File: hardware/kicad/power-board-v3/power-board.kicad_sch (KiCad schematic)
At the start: 5 parts

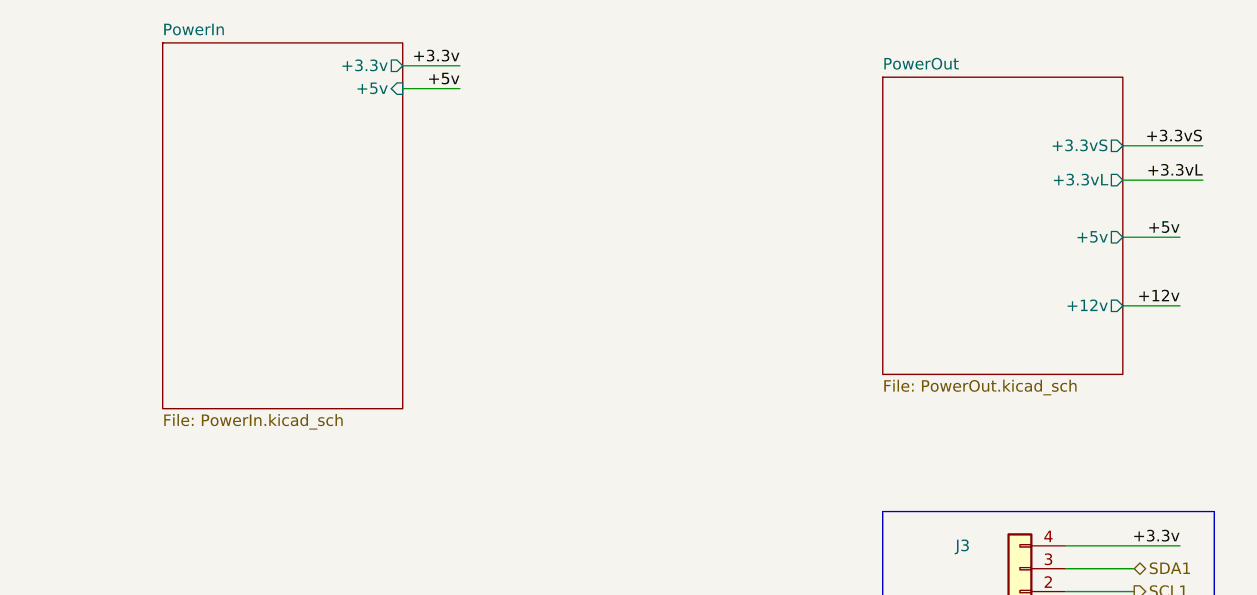
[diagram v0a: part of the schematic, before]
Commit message: add power balance and regulator
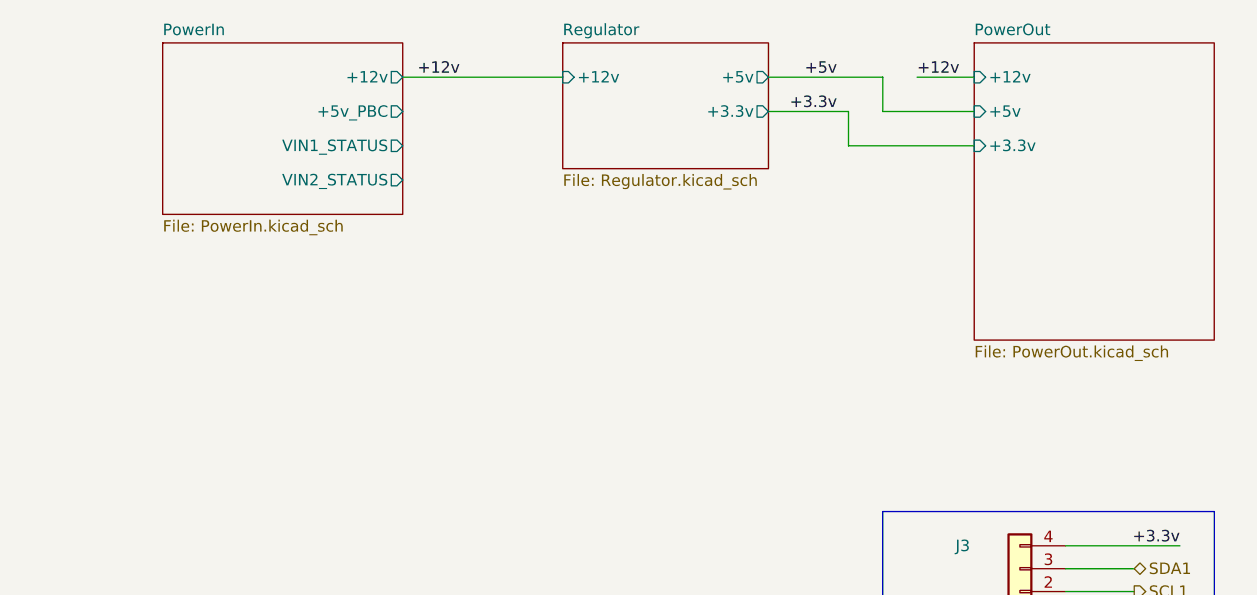
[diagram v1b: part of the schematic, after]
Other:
- added sheet Regulator (Regulator.kicad_sch)
- sheet PowerIn ports: added +12v, +5v_PBC, VIN1_STATUS, VIN2_STATUS; removed +3.3v, +5v
- sheet PowerOut ports: added +3.3v; removed +3.3vL, +3.3vS

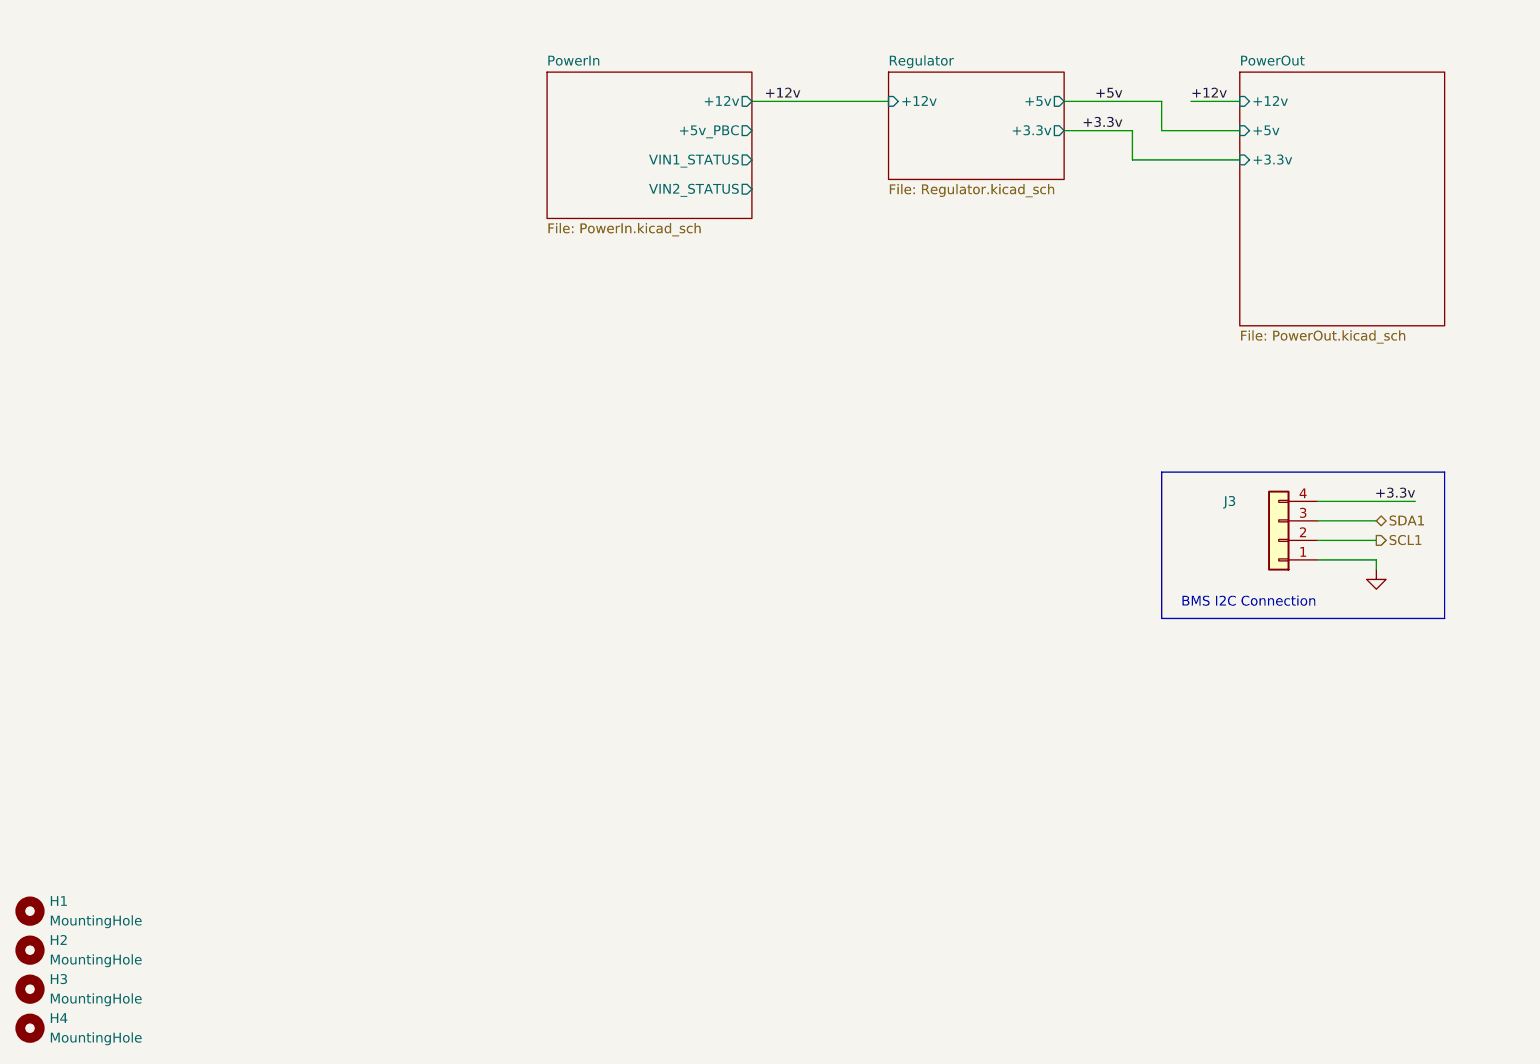
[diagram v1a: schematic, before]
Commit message: add base symbol and wiring
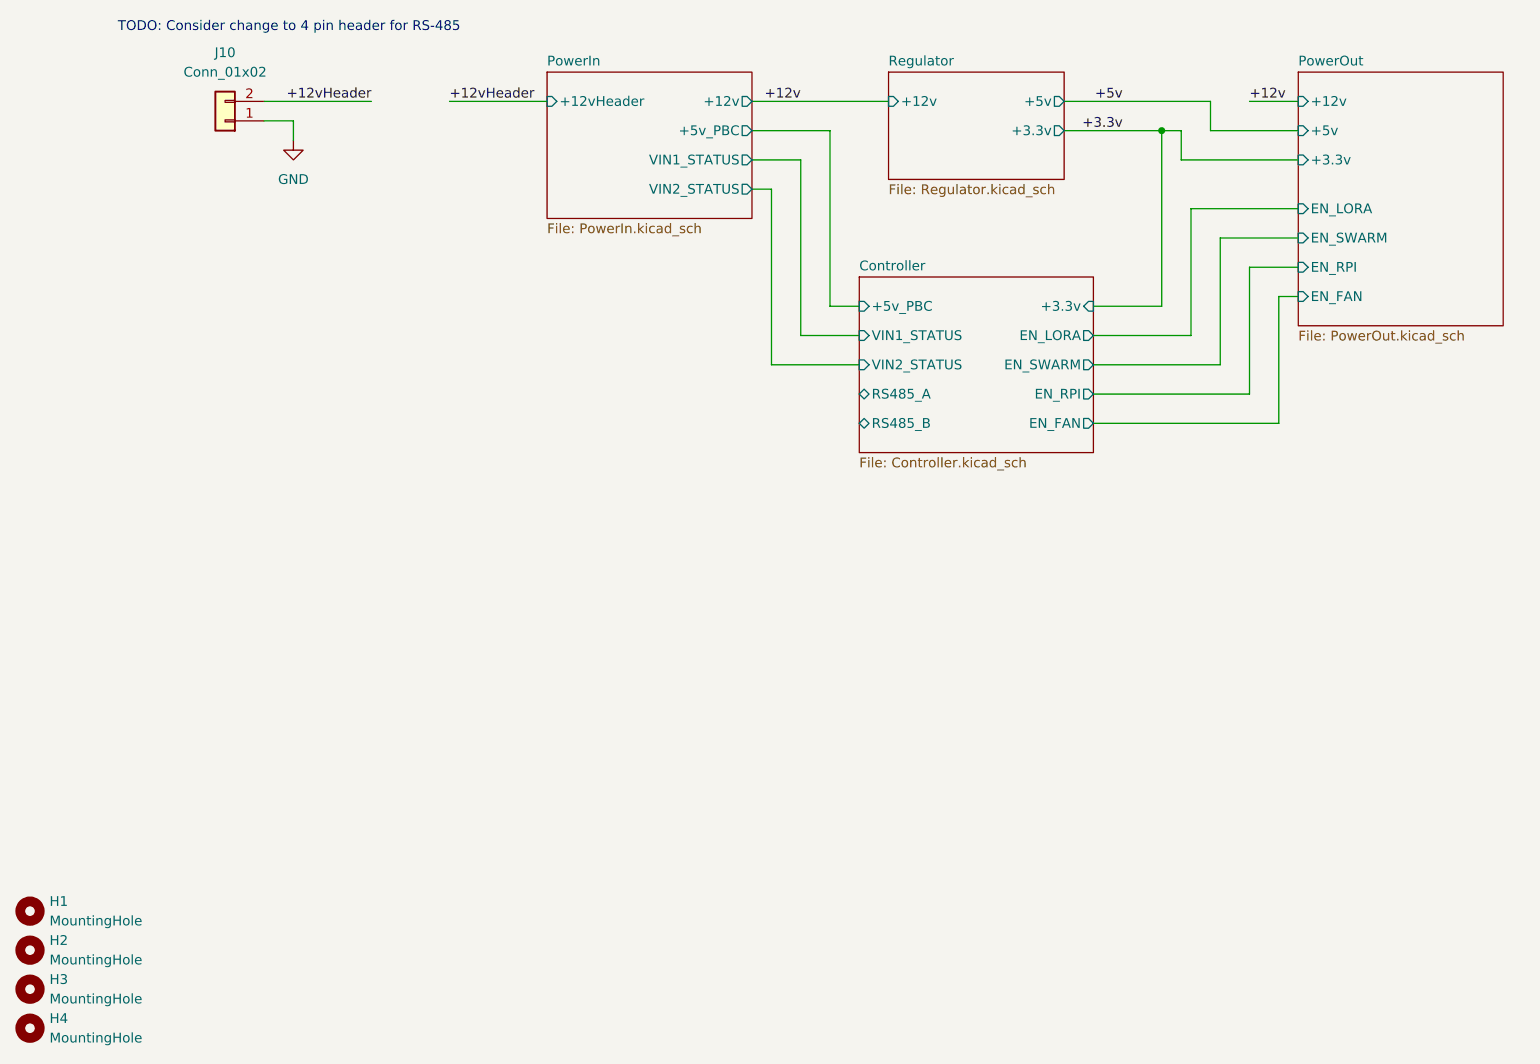
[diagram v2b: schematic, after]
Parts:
- removed J3: ~, Connector_PinSocket_2.54mm:PinSocket_1x04_P2.54mm_Vertical, symbol Connector_Generic:Conn_01x04
- added J10: Conn_01x02, Teapot:Molex_Micro-Fit_3.0_43650-0200_1x02_P3.00mm_Horizontal, symbol Connector_Generic:Conn_01x02
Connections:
- net GND: now also J10.1 (Pin_1)
- new net +12vHeader: J10.2 (Pin_2)
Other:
- added sheet Controller (Controller.kicad_sch)
- sheet PowerIn ports: added +12vHeader; removed none
- sheet PowerOut ports: added EN_FAN, EN_LORA, EN_RPI, EN_SWARM; removed none
- note added: "TODO: Consider change to 4 pin header for RS-485"
- note removed: "BMS I2C Connection"

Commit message: initial controller design
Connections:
- net +12vHeader renamed +12v_Header
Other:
- sheet PowerIn ports: added +12v_Header; removed +12vHeader
